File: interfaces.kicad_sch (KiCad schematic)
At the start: 96 parts, among them IC3 TPD8S009DSMR, J4 WE_629105150521, J6 685119134923, J7 1140084168, Q2 BSS138APW, Q3 BSS138APW, Q4 BSS138APW, Q5 BSS138APW, Q6 BSS138APW, U7 FT4232HQ, Y2 ABM8G-12.000MHZ-18-D2Y-T

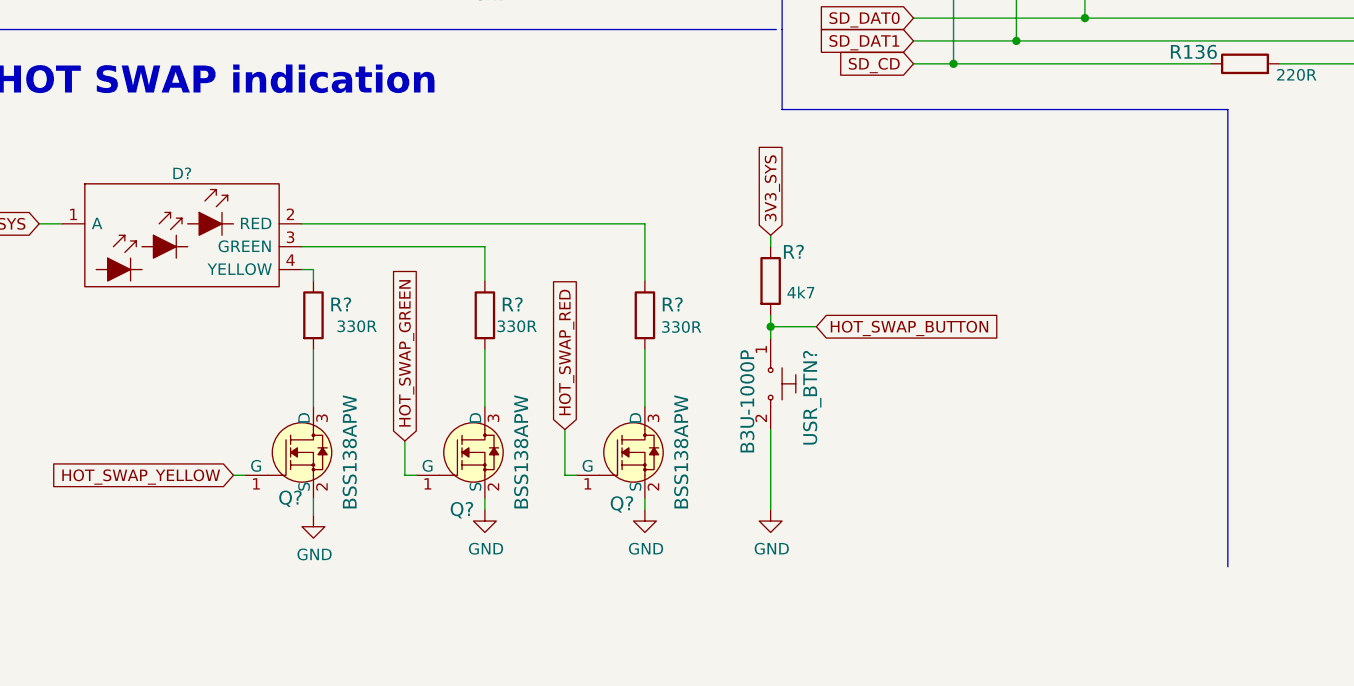
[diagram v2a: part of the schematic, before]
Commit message: Connect ETH mux, connect AUX_JTAG to FMC connector, add RC filter for HOT_SWAP_BUTTON signal
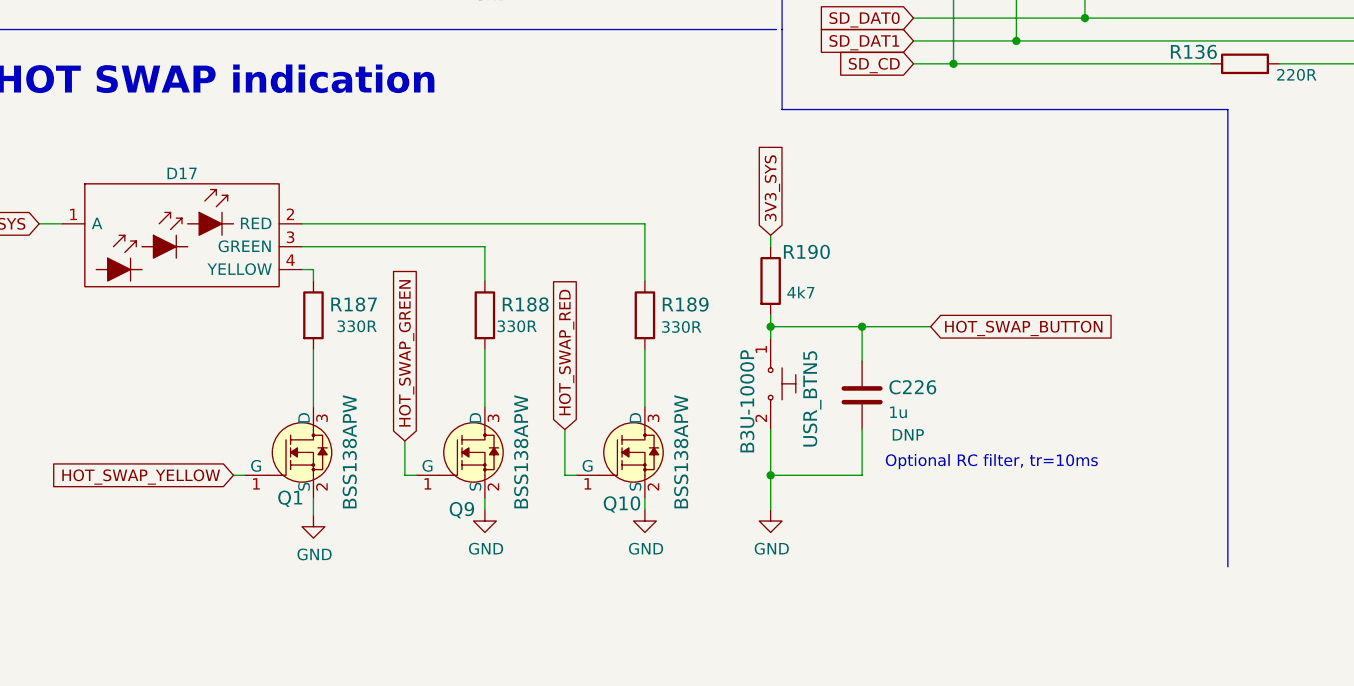
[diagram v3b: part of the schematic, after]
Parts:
- added C226: C_1u_0402, antmicro-footprints:0402-cap, symbol antmicroCapacitors0402:C_1u_0402
- gave numbers to parts that had none: 9
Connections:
- net GND: now also C226.2
- net HOT_SWAP_BUTTON: now also C226.1
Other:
- note added: "Optional RC filter, tr=10ms"
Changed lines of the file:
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@@
   (junction (at 95.885 157.48) (diameter 0) (color 0 0 0 0)
   )
+  (junction (at 309.88 226.06) (diameter 0) (color 0 0 0 0)
+  )
   (junction (at 41.91 104.14) (diameter 0) (color 0 0 0 0)
   )
@@
   (junction (at 48.895 104.14) (diameter 0) (color 0 0 0 0)
   )
+  (junction (at 299.72 242.57) (diameter 0) (color 0 0 0 0)
+  )
   (junction (at 370.84 158.115) (diameter 0) (color 0 0 0 0)
   )
@@
     (stroke (width 0) (type default) (color 0 0 0 0))
   )
+  (wire (pts (xy 309.88 242.57) (xy 309.88 237.49))
+    (stroke (width 0) (type default) (color 0 0 0 0))
+  )
   (wire (pts (xy 306.07 81.28) (xy 306.07 66.04))
     (stroke (width 0) (type default) (color 0 0 0 0))
@@
     (stroke (width 0) (type default) (color 0 0 0 0))
   )
-  (wire (pts (xy 299.72 226.06) (xy 304.8 226.06))
+  (wire (pts (xy 299.72 226.06) (xy 309.88 226.06))
     (stroke (width 0) (type default) (color 0 0 0 0))
   )
@@
     (stroke (width 0) (type default) (color 0 0 0 0))
   )
+  (wire (pts (xy 299.72 242.57) (xy 299.72 246.38))
+    (stroke (width 0) (type default) (color 0 0 0 0))
+  )
   (wire (pts (xy 160.655 142.24) (xy 160.655 144.78))
     (stroke (width 0) (type default) (color 0 0 0 0))
@@
     (stroke (width 0) (type default) (color 0 0 0 0))
   )
+  (wire (pts (xy 309.88 226.06) (xy 309.88 229.87))
+    (stroke (width 0) (type default) (color 0 0 0 0))
+  )
   (wire (pts (xy 248.92 228.6) (xy 248.92 234.95))
     (stroke (width 0) (type default) (color 0 0 0 0))
@@
     (stroke (width 0) (type default) (color 0 0 0 0))
   )
-  (wire (pts (xy 299.72 237.49) (xy 299.72 246.38))
+  (wire (pts (xy 299.72 237.49) (xy 299.72 242.57))
     (stroke (width 0) (type default) (color 0 0 0 0))
   )
@@
     (stroke (width 0) (type default) (color 0 0 0 0))
   )
+  (wire (pts (xy 309.88 226.06) (xy 317.5 226.06))
+    (stroke (width 0) (type default) (color 0 0 0 0))
+  )
   (wire (pts (xy 241.935 62.23) (xy 241.935 69.85))
     (stroke (width 0) (type default) (color 0 0 0 0))
@@
     (stroke (width 0) (type default) (color 0 0 0 0))
   )
+  (wire (pts (xy 299.72 242.57) (xy 309.88 242.57))
+    (stroke (width 0) (type default) (color 0 0 0 0))
+  )
   (wire (pts (xy 247.65 88.9) (xy 247.65 91.44))
     (stroke (width 0) (type default) (color 0 0 0 0))
@@
     (effects (font (size 2.9972 2.9972) (thickness 0.5994) bold) (justify left bottom))
   )
+  (text "Optional RC filter, tr=10ms" (at 312.42 241.935 0)
+    (effects (font (size 1.27 1.27)) (justify left bottom))
+  )
   (global_label "C_TMDS_D1_P" (shape input) (at 273.685 60.96 0) (fields_autoplaced)
     (effects (font (size 1.27 1.27)) (justify left))
@@
     )
   )
-  (global_label "HOT_SWAP_BUTTON" (shape input) (at 304.8 226.06 0) (fields_autoplaced)
+  (global_label "HOT_SWAP_BUTTON" (shape input) (at 317.5 226.06 0) (fields_autoplaced)
     (effects (font (size 1.27 1.27)) (justify left))
-    (property "Intersheet References" "${INTERSHEET_REFS}" (id 0) (at 324.9042 225.9806 0)
+    (property "Intersheet References" "${INTERSHEET_REFS}" (id 0) (at 337.6042 225.9806 0)
       (effects (font (size 1.27 1.27)) (justify left) hide)
     )
@@
   (symbol (lib_id "data-center-dram-tester:BSS138APW") (at 267.97 240.03 0) (unit 1)
     (in_bom yes) (on_board yes)
-    (property "Reference" "Q?" (id 0) (at 265.43 246.38 0)
+    (property "Reference" "Q9" (id 0) (at 265.43 246.38 0)
       (effects (font (size 1.524 1.524)))
     )
@@
   (symbol (lib_id "data-center-dram-tester:R_4k7_0402") (at 299.72 220.98 270) (unit 1)
     (in_bom yes) (on_board yes)
-    (property "Reference" "R?" (id 0) (at 300.99 217.805 90)
+    (property "Reference" "R190" (id 0) (at 300.99 217.805 90)
       (effects (font (size 1.524 1.524)) (justify left))
     )
@@
   (symbol (lib_id "data-center-dram-tester:R_330R_0402") (at 248.92 224.79 270) (unit 1)
     (in_bom yes) (on_board yes)
-    (property "Reference" "R?" (id 0) (at 250.698 223.647 90)
+    (property "Reference" "R187" (id 0) (at 250.698 223.647 90)
       (effects (font (size 1.524 1.524)) (justify left))
     )
@@
   (symbol (lib_id "data-center-dram-tester:B3U-1000P") (at 299.72 232.41 270) (unit 1)
     (in_bom yes) (on_board yes)
-    (property "Reference" "USR_BTN?" (id 0) (at 304.165 228.6 0)
+    (property "Reference" "USR_BTN5" (id 0) (at 304.165 228.6 0)
       (effects (font (size 1.524 1.524)) (justify left))
     )
@@
   (symbol (lib_id "data-center-dram-tester:R_330R_0402") (at 285.75 224.79 270) (unit 1)
     (in_bom yes) (on_board yes)
-    (property "Reference" "R?" (id 0) (at 287.528 223.647 90)
+    (property "Reference" "R189" (id 0) (at 287.528 223.647 90)
       (effects (font (size 1.524 1.524)) (justify left))
     )
@@
     (pin "2")
   )
+  (symbol (lib_id "antmicroCapacitors0402:C_1u_0402") (at 309.88 233.68 0) (unit 1)
+    (in_bom yes) (on_board yes)
+    (property "Reference" "C226" (id 0) (at 312.801 232.8454 0)
+      (effects (font (size 1.524 1.524)) (justify left))
+    )
+    (property "Value" "C_1u_0402" (id 1) (at 309.88 237.49 0)
+      (effects (font (size 1.524 1.524)) hide)
+    )
+    (property "Footprint" "antmicro-footprints:0402-cap" (id 2) (at 314.96 228.6 0)
+      (effects (font (size 1.524 1.524)) (justify left) hide)
+    )
+    (property "Datasheet" "" (id 3) (at 309.88 233.68 0)
+      (effects (font (size 1.27 1.27)) hide)
+    )
+    (property "Manufacturer" "TDK" (id 4) (at 314.96 223.52 0)
+      (effects (font (size 1.524 1.524)) (justify left) hide)
+    )
+    (property "MPN" "C1005X6S1A105K050BC" (id 5) (at 314.96 226.06 0)
+      (effects (font (size 1.524 1.524)) (justify left) hide)
+    )
+    (property "Val" "1u" (id 6) (at 312.801 235.6105 0)
+      (effects (font (size 1.27 1.27)) (justify left))
+    )
+    (property "DNP" "DNP" (id 7) (at 314.96 238.125 0))
+    (pin "1")
+    (pin "2")
+  )
   (symbol (lib_id "antmicroLEDIndicationDiscrete:APTF1616SURKCGKSYKC") (at 223.52 210.82 0) (unit 1)
     (in_bom yes) (on_board yes) (fields_autoplaced)
-    (property "Reference" "D?" (id 0) (at 234.315 209.073 0))
+    (property "Reference" "D17" (id 0) (at 234.315 209.073 0))
     (property "Value" "APTF1616SURKCGKSYKC" (id 1) (at 257.81 214.63 0)
       (effects (font (size 1.27 1.27)) (justify left) hide)
@@
   (symbol (lib_id "data-center-dram-tester:R_330R_0402") (at 267.97 224.79 270) (unit 1)
     (in_bom yes) (on_board yes)
-    (property "Reference" "R?" (id 0) (at 269.748 223.647 90)
+    (property "Reference" "R188" (id 0) (at 269.748 223.647 90)
       (effects (font (size 1.524 1.524)) (justify left))
     )
@@
   (symbol (lib_id "data-center-dram-tester:BSS138APW") (at 248.92 240.03 0) (unit 1)
     (in_bom yes) (on_board yes)
-    (property "Reference" "Q?" (id 0) (at 246.38 245.11 0)
+    (property "Reference" "Q1" (id 0) (at 246.38 245.11 0)
       (effects (font (size 1.524 1.524)))
     )
@@
   (symbol (lib_id "data-center-dram-tester:GND") (at 248.92 247.015 0) (unit 1)
     (in_bom yes) (on_board yes)
-    (property "Reference" "#PWR?" (id 0) (at 248.92 253.365 0)
+    (property "Reference" "#PWR0323" (id 0) (at 248.92 253.365 0)
       (effects (font (size 1.27 1.27)) hide)
     )
@@
   (symbol (lib_id "data-center-dram-tester:GND") (at 299.72 246.38 0) (unit 1)
     (in_bom yes) (on_board yes)
-    (property "Reference" "#PWR?" (id 0) (at 299.72 252.73 0)
+    (property "Reference" "#PWR0324" (id 0) (at 299.72 252.73 0)
       (effects (font (size 1.27 1.27)) hide)
     )
@@
   (symbol (lib_id "data-center-dram-tester:GND") (at 267.97 246.38 0) (unit 1)
     (in_bom yes) (on_board yes)
-    (property "Reference" "#PWR?" (id 0) (at 267.97 252.73 0)
+    (property "Reference" "#PWR0321" (id 0) (at 267.97 252.73 0)
       (effects (font (size 1.27 1.27)) hide)
     )
@@
   (symbol (lib_id "data-center-dram-tester:GND") (at 285.75 246.38 0) (unit 1)
     (in_bom yes) (on_board yes)
-    (property "Reference" "#PWR?" (id 0) (at 285.75 252.73 0)
+    (property "Reference" "#PWR0322" (id 0) (at 285.75 252.73 0)
       (effects (font (size 1.27 1.27)) hide)
     )
@@
   (symbol (lib_id "data-center-dram-tester:BSS138APW") (at 285.75 240.03 0) (unit 1)
     (in_bom yes) (on_board yes)
-    (property "Reference" "Q?" (id 0) (at 283.21 245.745 0)
+    (property "Reference" "Q10" (id 0) (at 283.21 245.745 0)
       (effects (font (size 1.524 1.524)))
     )

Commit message: Implement LED and PB mechanical concept. Assign bank 15 to FMC, remove buttons and add new ones
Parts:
- removed J7: 1140084168, data-center-dram-tester-footprints:MicroSD_1140084168, symbol data-center-dram-tester:1140084168
- removed R15, R16, R17, R29: R_4k7_0402, data-center-dram-tester-footprints:0402-res, symbol data-center-dram-tester:R_4k7_0402
- removed USR_BTN1, USR_BTN2, USR_BTN3, USR_BTN4: B3U-1000P, data-center-dram-tester-footprints:Switch_Tactile_SMD_B3U-1000P, symbol data-center-dram-tester:B3U-1000P
- added J9: DM3AT-SF-PEJM5, antmicro-footprints:MicroSD_DM3AT-SF-PEJM5, symbol antmicroMemoryConnectorsPCCardSockets:DM3AT-SF-PEJM5
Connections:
- net 3V3_SYS: now also J9.4 (VDD)
- net GND: now also J9.11 (SHIELD), J9.6 (VSS), J9.9 (DET_B)
- net SD_CLK: now also J9.5 (CLK)
- net SD_CMD: now also J9.3 (CMD)
- net SD_DAT0: now also J9.7 (DAT0)
- net SD_DAT1: now also J9.8 (DAT1)
- net SD_DAT2: now also J9.1 (DAT2)
- net SD_DAT3: now also J9.2 (DAT3/CD)
- net at R136.2: now also J9.10 (DET_A)
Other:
- note removed: "User buttons"
- moved on the sheet: C10, R132, R133, R134, R135, R136, R137, R138

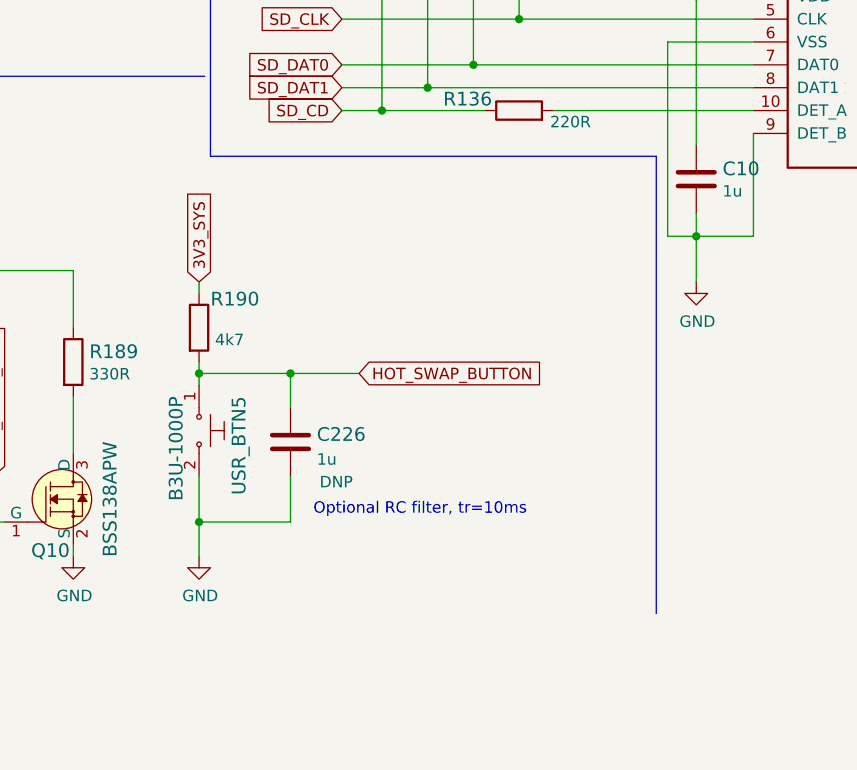
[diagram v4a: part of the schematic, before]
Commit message: Improve mechanical concept
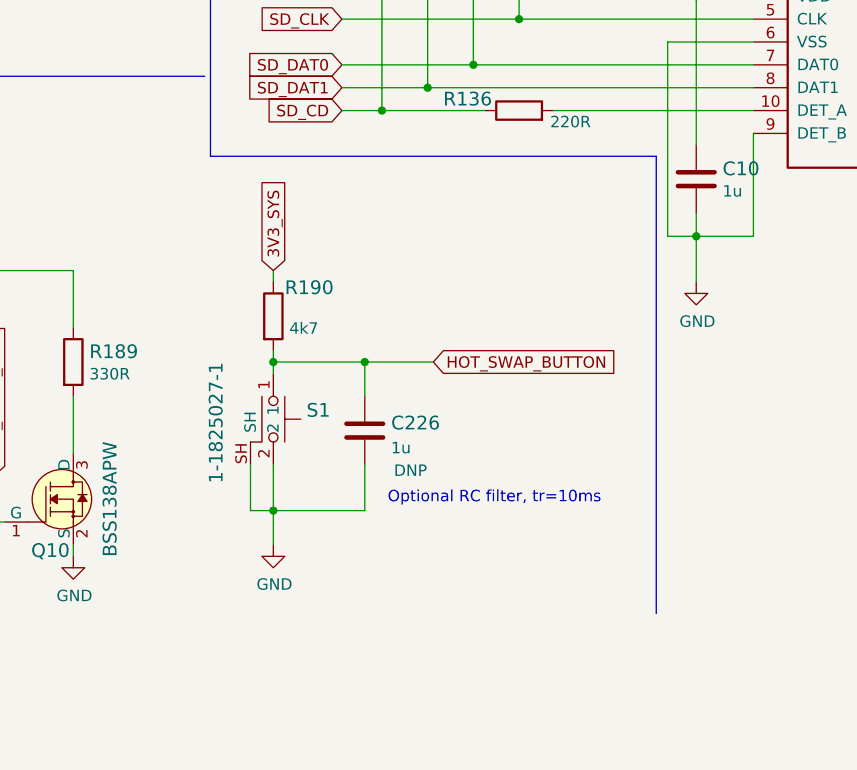
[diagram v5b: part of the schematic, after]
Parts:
- removed USR_BTN5: B3U-1000P, data-center-dram-tester-footprints:Switch_Tactile_SMD_B3U-1000P, symbol data-center-dram-tester:B3U-1000P
- added S1: 1-1825027-1, antmicro-footprints:TE_1-1825027-1, symbol antmicroTactileSwitches:1-1825027-1
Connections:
- net GND: now also S1.2, S1.SH
- net HOT_SWAP_BUTTON: now also S1.1
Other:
- moved on the sheet: C226, R190

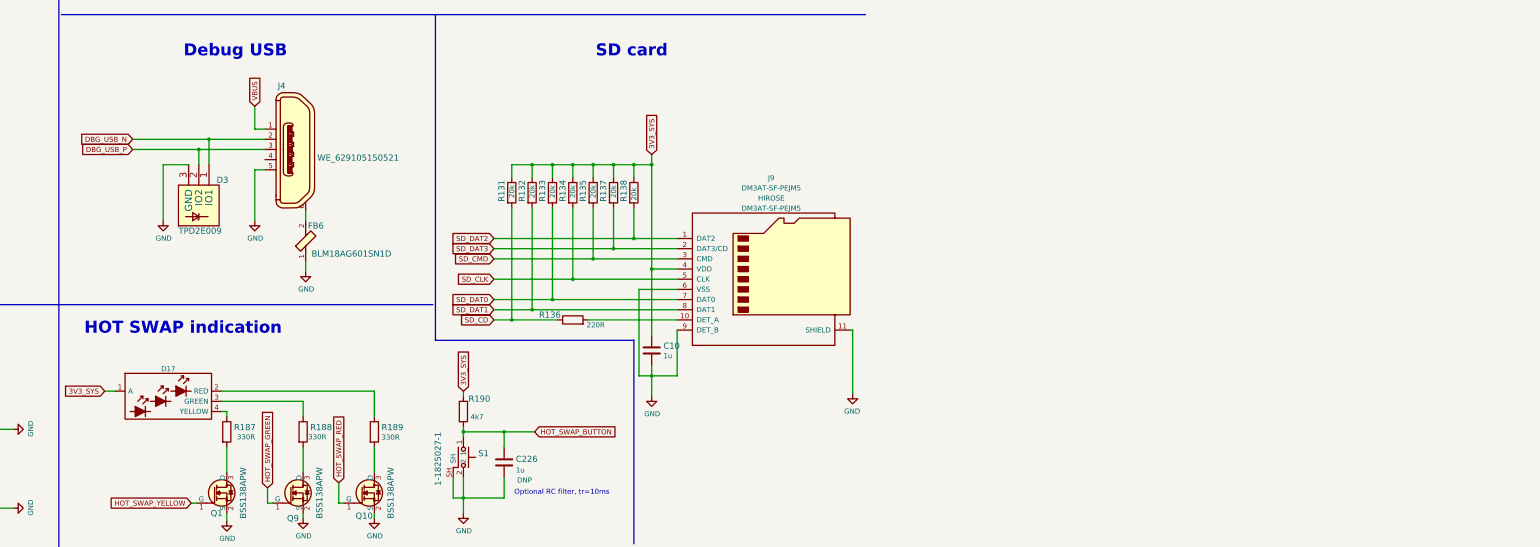
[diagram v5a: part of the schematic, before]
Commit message: Finish mechanical concept, add active capacitor discharge circuit for all AP DC-DC, add pushbutton controler circuit
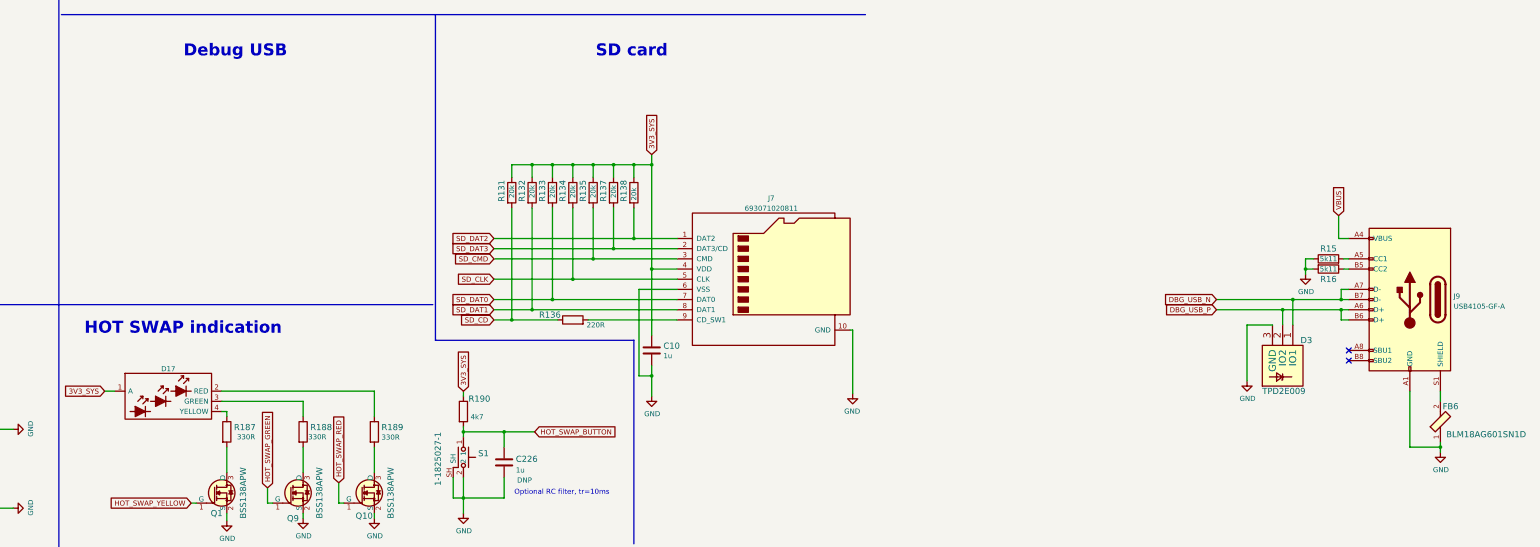
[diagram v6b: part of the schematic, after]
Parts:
- removed J4: WE_629105150521, data-center-dram-tester-footprints:USB_Micro_B_Female_629105150521, symbol data-center-dram-tester:WE_629105150521
- removed J9: DM3AT-SF-PEJM5, antmicro-footprints:MicroSD_DM3AT-SF-PEJM5, symbol antmicroMemoryConnectorsPCCardSockets:DM3AT-SF-PEJM5
- added J7: 693071020811, antmicro-footprints:WE_693071020811, symbol antmicroMemoryConnectorsPCCardSockets:693071020811
- added J9: USB4105-GF-A, antmicro-footprints:GCT_USB4105-GF-A, symbol antmicroUSBDVIHDMIConnectors:USB4105-GF-A
- added R15, R16: R_5k11_0402, antmicro-footprints:0402-res, symbol antmicroResistors0402:R_5k11_0402
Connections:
- net 3V3_SYS: now also J7.4 (VDD)
- net DBG_USB_N: now also J9.A7 (D-), J9.B7 (D-)
- net DBG_USB_P: now also J9.A6 (D+), J9.B6 (D+)
- net GND: now also J7.10 (GND), J7.11 (GND), J7.12 (GND), J7.13 (GND), J7.6 (VSS), J9.A1 (GND), J9.A12 (GND), J9.B1 (GND), J9.B12 (GND), R15.1, R16.2
- net SD_CLK: now also J7.5 (CLK)
- net SD_CMD: now also J7.3 (CMD)
- net SD_DAT0: now also J7.7 (DAT0)
- net SD_DAT1: now also J7.8 (DAT1)
- net SD_DAT2: now also J7.1 (DAT2)
- net SD_DAT3: now also J7.2 (DAT3/CD)
- net VBUS: now also J9.A4 (VBUS), J9.A9 (VBUS), J9.B4 (VBUS), J9.B9 (VBUS)
- net at FB6.2: now also J9.S1 (SHIELD)
- net at R136.2: now also J7.9 (CD_SW1)
- new net: J9.A5 (CC1), R15.2
- new net: J9.B5 (CC2), R16.1
- no-connect marks 7 -> 9
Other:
- moved on the sheet: D3, FB6

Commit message: Cleanup schematic
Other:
- note added: "HOT SWAP eject button"
- note added: "HOT SWAP status LED"
- note removed: "HOT SWAP indication"
- moved on the sheet: C226, D17, D3, D5, D6, D7, D8, D9, FB6, J9, Q1, Q10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
